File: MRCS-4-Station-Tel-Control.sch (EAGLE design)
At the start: 4 parts

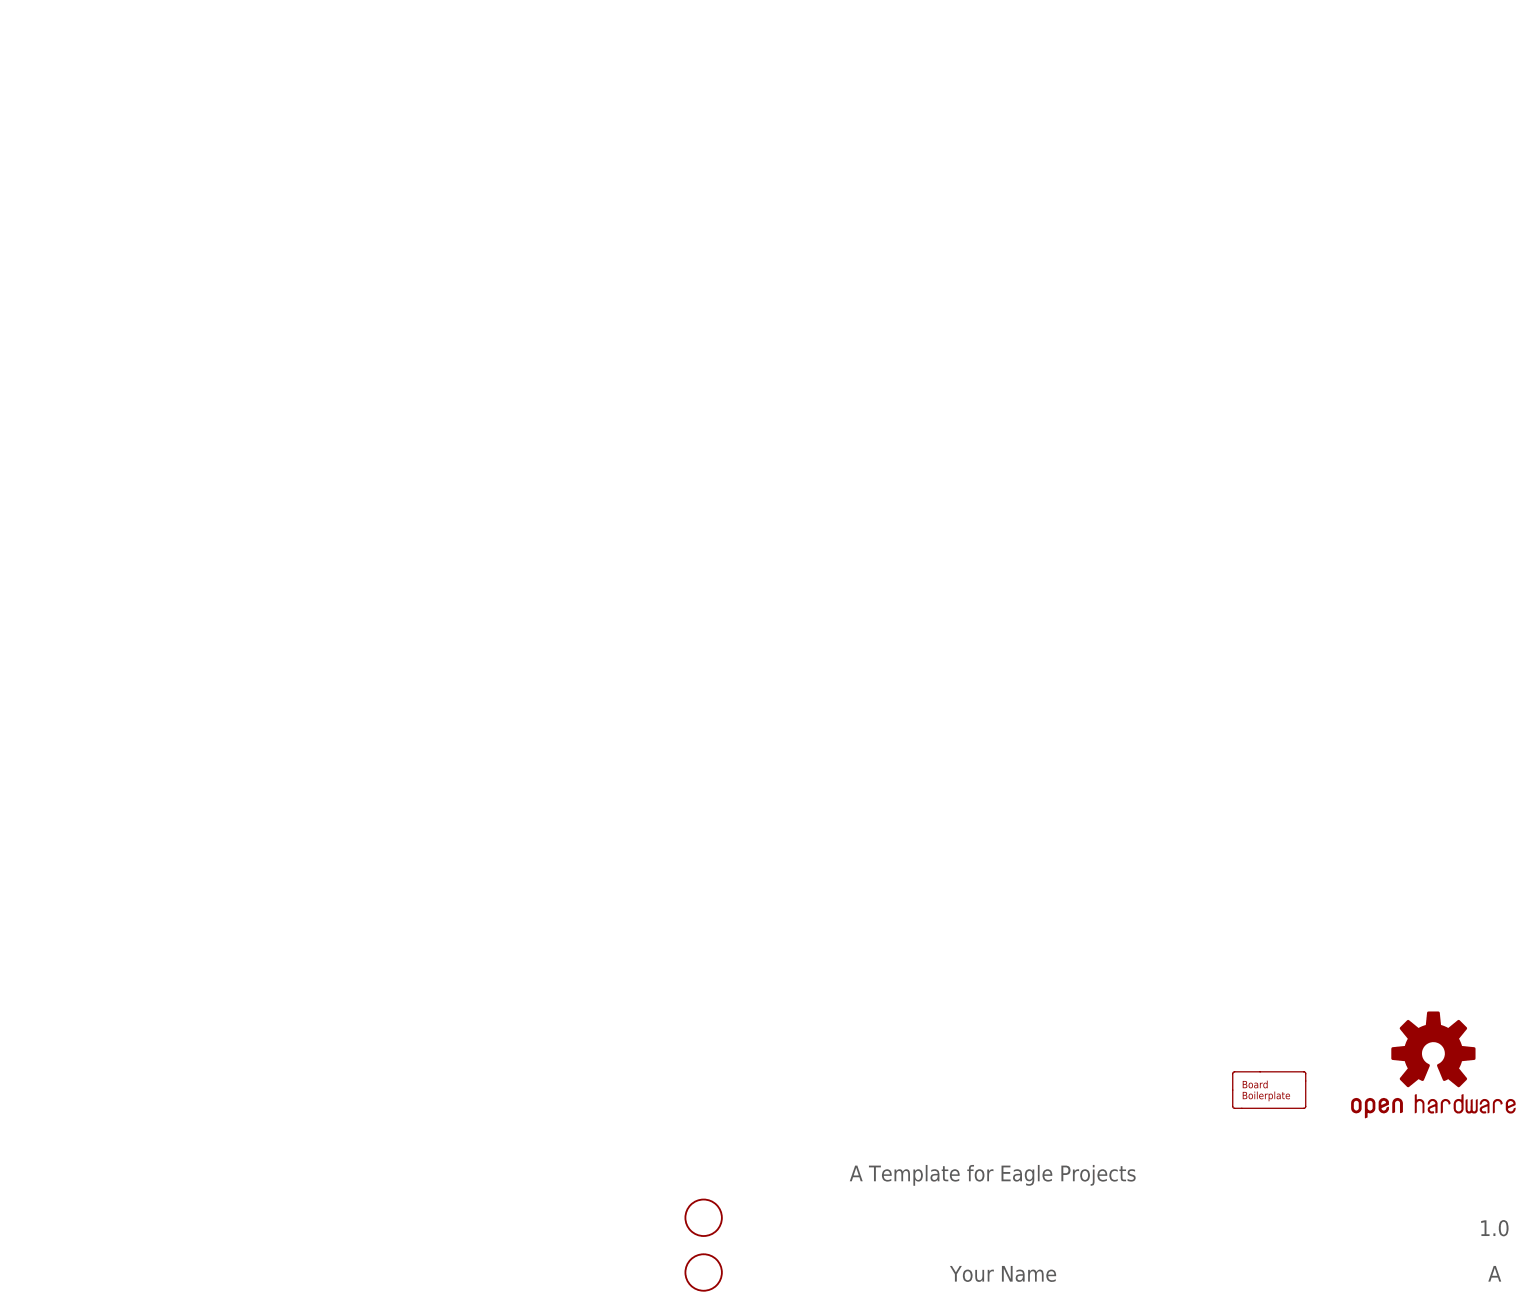
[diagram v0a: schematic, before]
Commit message: First pass of board complete
This is the first iteration of the board.
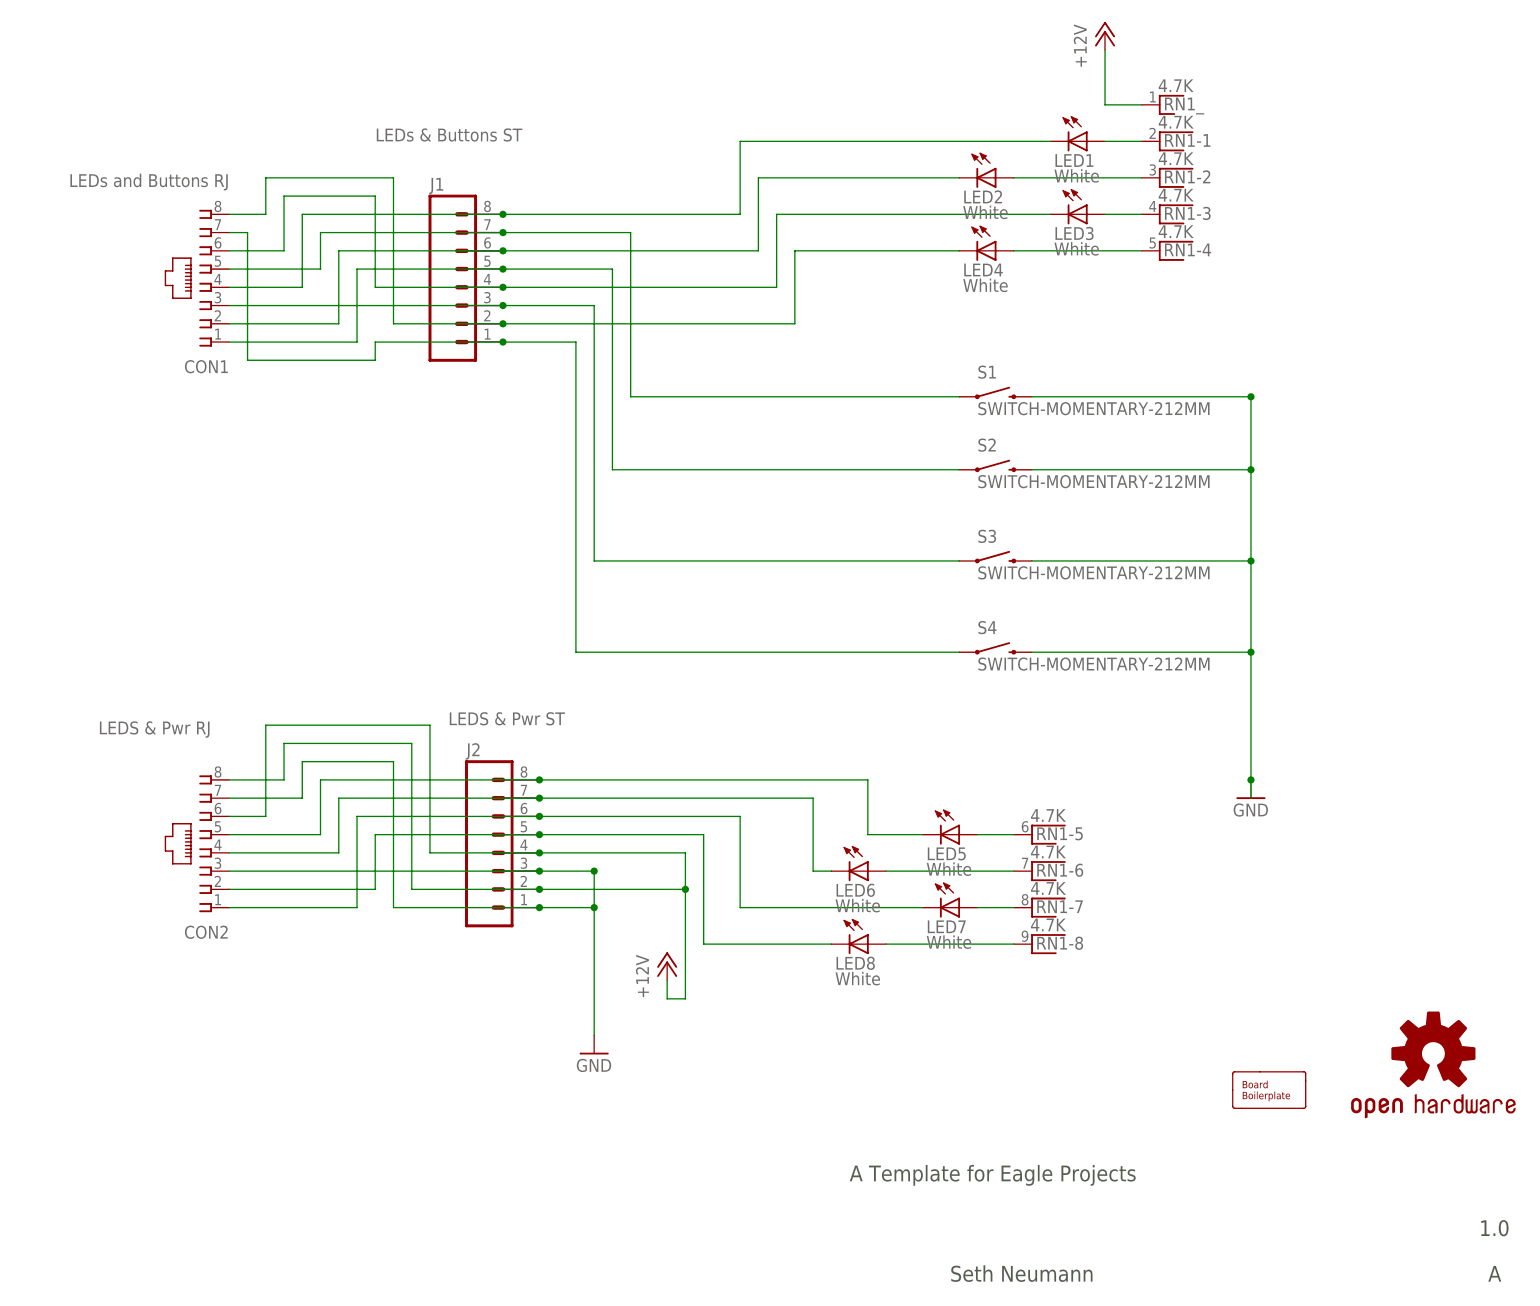
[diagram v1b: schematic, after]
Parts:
- removed FID1, FID2: FIDUCIAL, SPCoast:FIDUCIAL
- added CON1: LEDs and Buttons RJ, SPCoast:CONNECTOR-RJ45-FRONT
- added CON2: LEDS & Pwr RJ, SPCoast:CONNECTOR-RJ45-FRONT
- added J1: LEDs & Buttons ST, SPCoast:CONNECTOR-M08LOCK
- added J2: LEDS & Pwr ST, SPCoast:CONNECTOR-M08LOCK
- added LED1, LED2, LED3, LED4, LED5, LED6, LED7, LED8: White, SPCoast:LEDLED5MM
- added RN1: 4.7K, resistor-net:RNX8
- added S1, S2, S3, S4: SWITCH-MOMENTARY-212MM, SparkFun-Electromechanical:SWITCH-MOMENTARY-212MM
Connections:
- new net +12V: CON2.6, CON2.8, J2.2, J2.4, RN1_.1
- new net GND: CON2.3, CON2.7, J2.1, J2.3, S1.2, S2.2, S3.2, S4.2
- new net N$1: LED1.A, RN1-1.1
- new net N$12: CON1.1, J1.5, S2.1
- new net N$13: CON1.5, J1.7, S1.1
- new net N$14: CON1.3, J1.3, S3.1
- new net N$15: CON1.6, J1.4, LED3.C
- new net N$16: CON1.7, J1.1, S4.1
- new net N$17: CON1.8, J1.2, LED4.C
- new net N$18: CON1.2, J1.6, LED2.C
- new net N$2: LED2.A, RN1-2.1
- new net N$20: CON2.5, J2.8, LED5.C
- new net N$21: CON2.4, J2.7, LED6.C
- new net N$22: CON2.1, J2.6, LED7.C
- new net N$23: CON2.2, J2.5, LED8.C
- new net N$3: LED3.A, RN1-3.1
- new net N$4: LED4.A, RN1-4.1
- new net N$5: LED5.A, RN1-5.1
- new net N$6: LED6.A, RN1-6.1
- new net N$7: LED7.A, RN1-7.1
- new net N$8: LED8.A, RN1-8.1
- new net N$9: CON1.4, J1.8, LED1.C
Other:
- note added: "Seth Neumann"
- note removed: "Your Name"
